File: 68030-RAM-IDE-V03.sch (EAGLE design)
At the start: 73 parts, among them IC1 REG1117, IC10 ICS570B, IC2 74HCT245PW, IC3 74AC16245, IC4 AM29F010S, IC5 74ALVT16543, IC6 74ALVT16543, IC7 XC95288XL-TQ144, IC8 K4S56163, IC9 K4S56163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

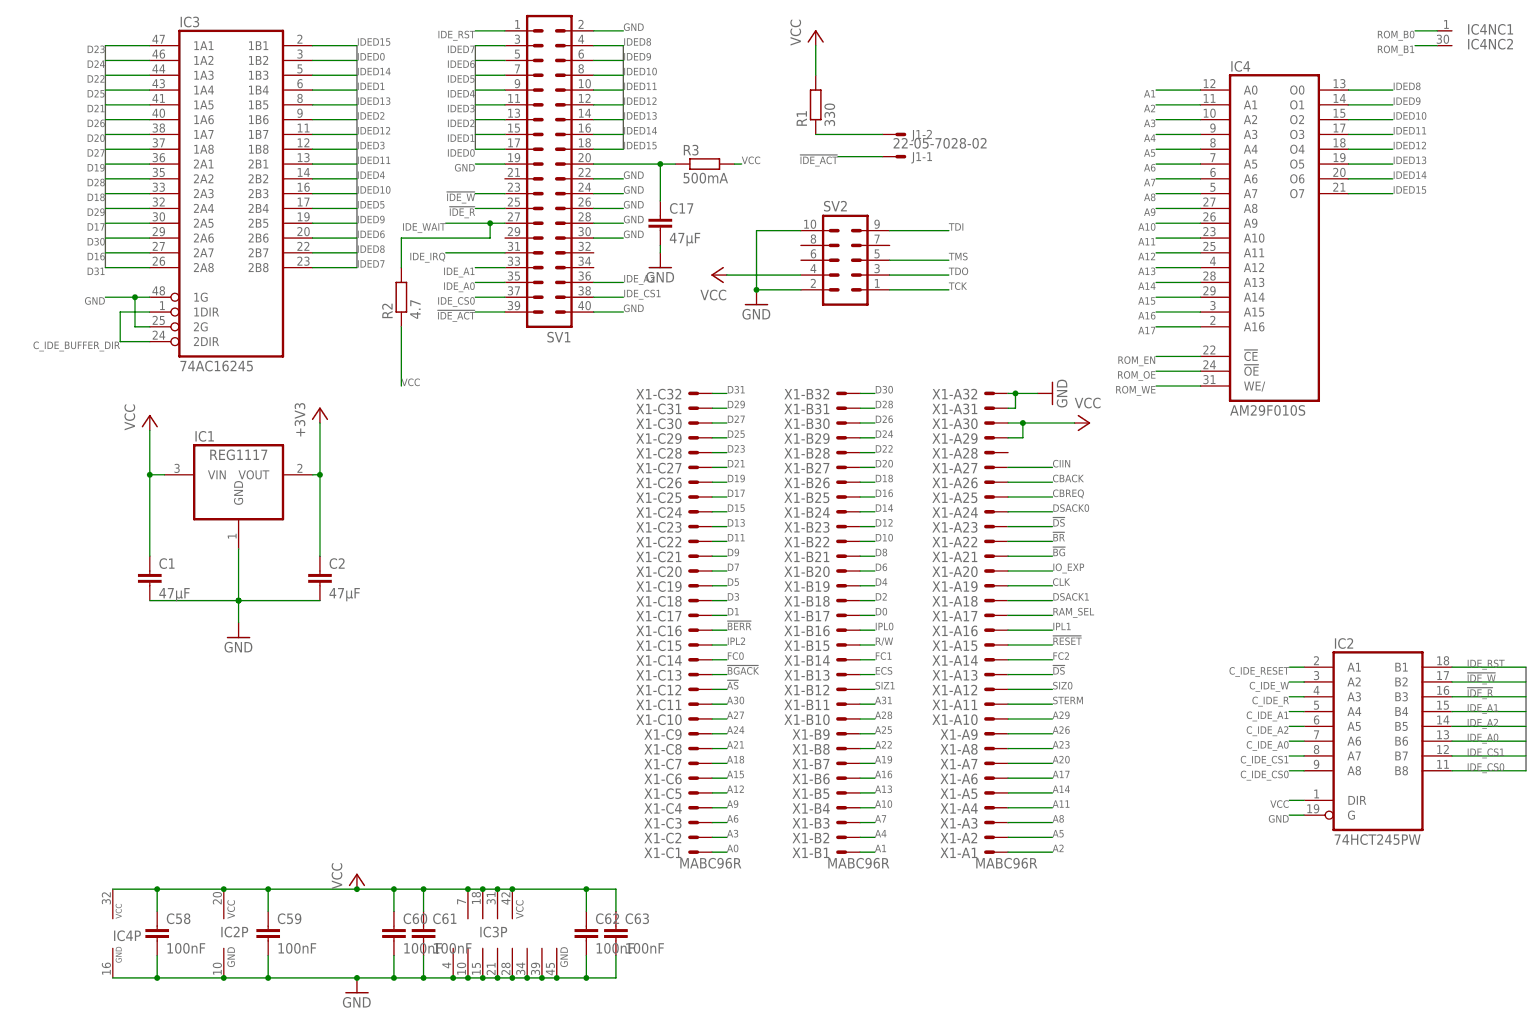
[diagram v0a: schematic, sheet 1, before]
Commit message: Cleaned ARAM/BA signals
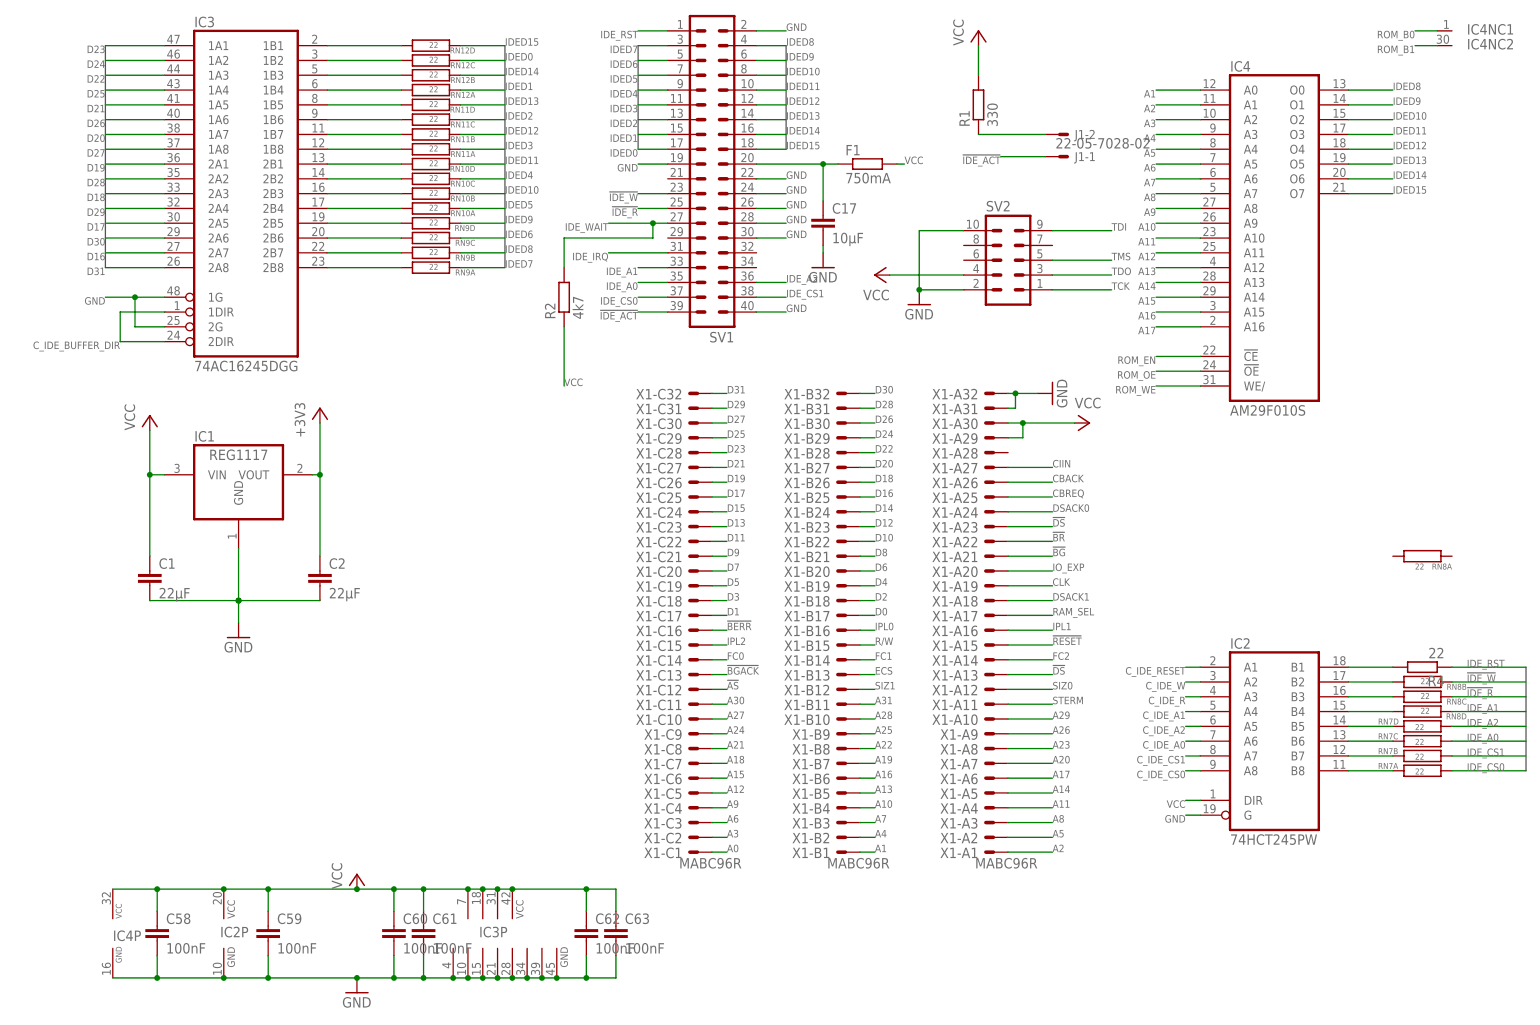
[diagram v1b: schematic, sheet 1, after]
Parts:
- removed R3: 500mA, rcl:R-EU_R2512
- added F1: 750mA, rcl:R-EU_R2512
- added RN1, RN10, RN11, RN12, RN7, RN8, RN9: 22, SMD:R-NETZ@3
- C1, C2: value 47µF -> 22µF; device rcl:C-EUC0805K -> rcl:C-EUC1210K
- C10, C11, C12, C13, C14, C15, C16, C3, C4, C5, C6, C7, C8, C9: device SMD:C-0805-K -> rcl:C-EUC0805K
- C17: value 47µF -> 10µF
- C18, C19, C20, C21, C22, C31, C32, C33, C34, C35, C37, C38, C58, C59, C60, C61, C62, C63: device rcl:C-EUC0603K -> rcl:C-EUC0805K
- C23, C24, C25, C26, C27, C28, C29, C30: value 10nF -> 100nF; device SMD:C-0603-K@3 -> rcl:C-EUC0805K
- C36: value (none) -> 100nF; device rcl:C-EUC0603K -> rcl:C-EUC0805K
- IC3: value 74AC16245 -> 74AC16245DGG; device 74ac-logic:74AC16245 -> 74ac-logic:74AC16245DGG
- IC5, IC6: value 74ALVT16543 -> 74LVTH16543
- R1, R10, R11, R12, R13: device rcl:R-EU_R0603 -> rcl:R-EU_R0805
- R2: value 4.7 -> 4k7; device rcl:R-EU_R0603 -> rcl:R-EU_R0805
- R4: value 33R -> 22; device SMD:R-NETZ@3 -> rcl:R-EU_R0805
- RN2, RN3, RN4, RN5, RN6: value 33R -> 22
- renumbered R5 to RN2, R6 to RN3, R7 to RN4, R8 to RN5, R9 to RN6
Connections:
- new net N$10: IC2A.B4, RN8D.P$1
- new net N$11: IC2A.B1, R4.2
- new net N$12: IC2A.B2, RN8B.P$1
- new net N$13: IC3G$1.1B3, RN12B.P$1
- new net N$14: IC3G$1.1B4, RN12A.P$1
- new net N$15: IC3G$1.1B1, RN12D.P$1
- new net N$16: IC3G$1.1B2, RN12C.P$1
- new net N$17: IC3G$1.1B7, RN11B.P$1
- new net N$18: IC3G$1.1B8, RN11A.P$1
- new net N$19: IC3G$1.1B5, RN11D.P$1
- new net N$2: IC2A.B7, RN7B.P$2
- new net N$20: IC3G$1.1B6, RN11C.P$1
- new net N$21: IC3G$1.2B3, RN10B.P$1
- new net N$22: IC3G$1.2B4, RN10A.P$1
- new net N$23: IC3G$1.2B1, RN10D.P$1
- new net N$24: IC3G$1.2B2, RN10C.P$1
- new net N$27: IC3G$1.2B7, RN9B.P$1
- new net N$28: IC3G$1.2B8, RN9A.P$1
- new net N$29: IC3G$1.2B5, RN9D.P$1
- new net N$3: IC2A.B8, RN7A.P$2
- new net N$30: IC3G$1.2B6, RN9C.P$1
- new net N$6: IC2A.B5, RN7D.P$2
- new net N$7: IC2A.B6, RN7C.P$2
- new net N$9: IC2A.B3, RN8C.P$1
- net !IDE_R: now also RN8C.P$2; no longer IC2A.B3
- net !IDE_W: now also RN8B.P$2; no longer IC2A.B2
- net ARAM_2: now also RN1B.P$1; no longer R4B.P$1
- net ARAM_3: now also RN1D.P$1; no longer R4D.P$1
- net ARAM_4: now also RN1C.P$1; no longer R4C.P$1
- net ARAM_5: now also RN1A.P$1; no longer R4A.P$1
- net C_ARAM_2: now also RN1B.P$2; no longer R4B.P$2
- net C_ARAM_3: now also RN1D.P$2; no longer R4D.P$2
- net C_ARAM_4: now also RN1C.P$2; no longer R4C.P$2
- net C_ARAM_5: now also RN1A.P$2; no longer R4A.P$2
- net IDED0: now also RN12C.P$2; no longer IC3G$1.1B2
- net IDED1: now also RN12A.P$2; no longer IC3G$1.1B4
- net IDED10: now also RN10B.P$2; no longer IC3G$1.2B3
- net IDED11: now also RN10D.P$2; no longer IC3G$1.2B1
- net IDED12: now also RN11B.P$2; no longer IC3G$1.1B7
- net IDED13: now also RN11D.P$2; no longer IC3G$1.1B5
- net IDED14: now also RN12B.P$2; no longer IC3G$1.1B3
- net IDED15: now also RN12D.P$2; no longer IC3G$1.1B1
- net IDED2: now also RN11C.P$2; no longer IC3G$1.1B6
- net IDED3: now also RN11A.P$2; no longer IC3G$1.1B8
- net IDED4: now also RN10C.P$2; no longer IC3G$1.2B2
- net IDED5: now also RN10A.P$2; no longer IC3G$1.2B4
- net IDED6: now also RN9C.P$2; no longer IC3G$1.2B6
- net IDED7: now also RN9A.P$2; no longer IC3G$1.2B8
- net IDED8: now also RN9B.P$2; no longer IC3G$1.2B7
- net IDED9: now also RN9D.P$2; no longer IC3G$1.2B5
- net IDE_A0: now also RN7C.P$1; no longer IC2A.B6
- net IDE_A1: now also RN8D.P$2; no longer IC2A.B4
- net IDE_A2: now also RN7D.P$1; no longer IC2A.B5
- net IDE_CS0: now also RN7A.P$1; no longer IC2A.B8
- net IDE_CS1: now also RN7B.P$1; no longer IC2A.B7
- net IDE_RST: now also R4.1; no longer IC2A.B1
- net IO_EXP: no longer IC7.P$38-FB5MC08/GCK3
- net KEY_PIN_POWER: now also F1.1; no longer R3.1
- net PLL_CLK_FULL: now also IC7.P$38-FB5MC08/GCK3
- net VCC: now also F1.2; no longer R3.2
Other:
- moved on the sheet: C10, C11, C12, C13, C14, C15, C16, C17, C23, C24, C25, C26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

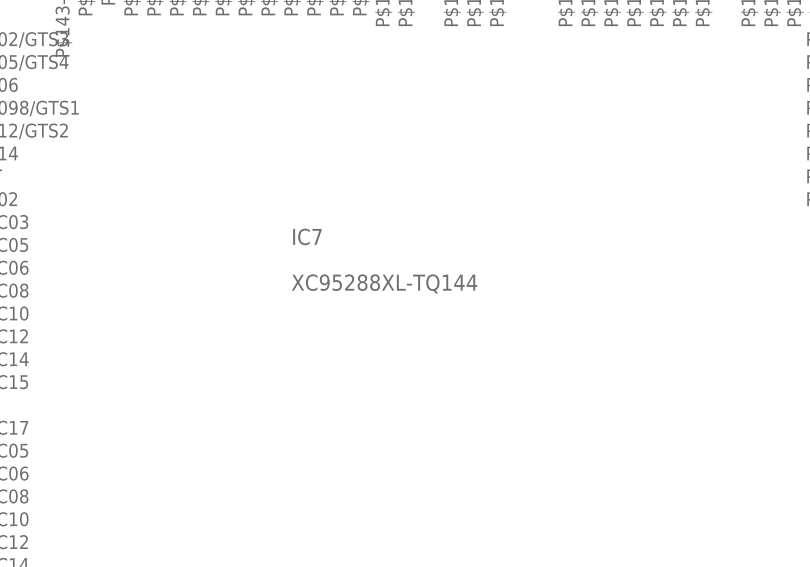
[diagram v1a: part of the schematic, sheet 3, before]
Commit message: Updated the schematics for actual parts
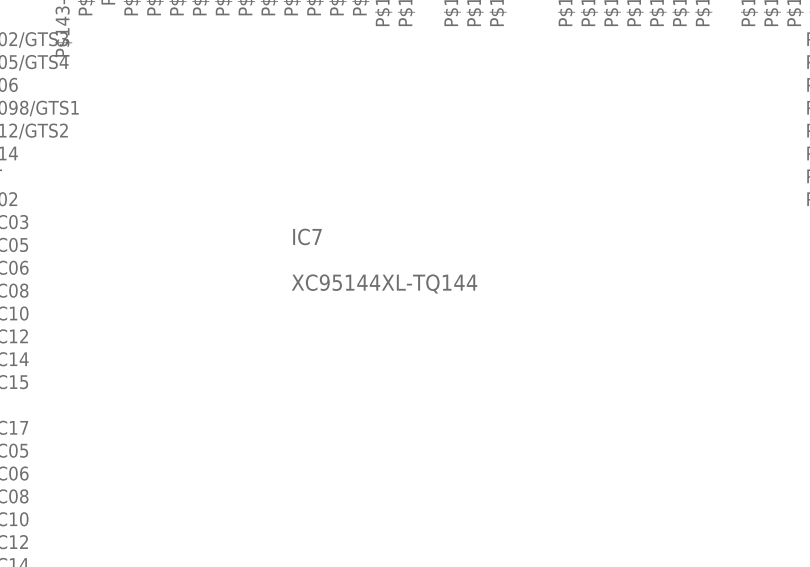
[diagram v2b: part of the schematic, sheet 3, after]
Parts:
- IC7: value XC95288XL-TQ144 -> XC95144XL-TQ144
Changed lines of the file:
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@@
 <part name="GND10" library="SUPPLY1" deviceset="GND" device=""/>
 <part name="IC1" library="burr-brown" deviceset="REG1117" device=""/>
-<part name="IC7" library="xilinx_xc9572xl-tq100" deviceset="XC95288XL-TQ144" device=""/>
+<part name="IC7" library="xilinx_xc9572xl-tq100" deviceset="XC95288XL-TQ144" device="" value="XC95144XL-TQ144"/>
 <part name="C18" library="rcl" deviceset="C-EU" device="C0805K" value="100nF"/>
 <part name="C19" library="rcl" deviceset="C-EU" device="C0805K" value="100nF"/>

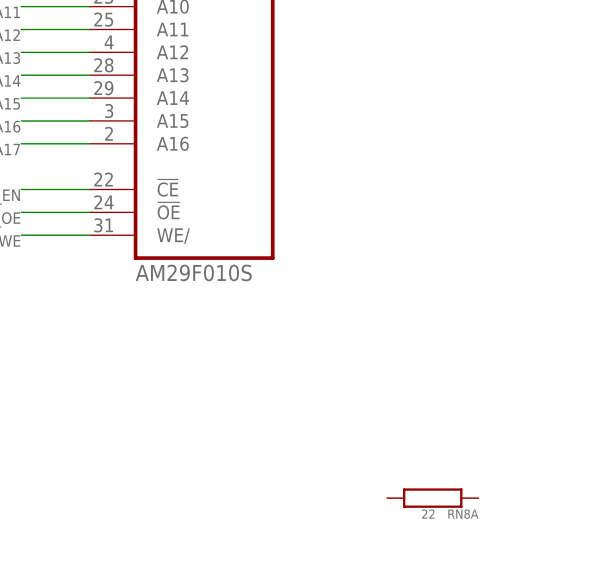
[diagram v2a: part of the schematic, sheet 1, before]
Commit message: Added a JTAG-Pullup
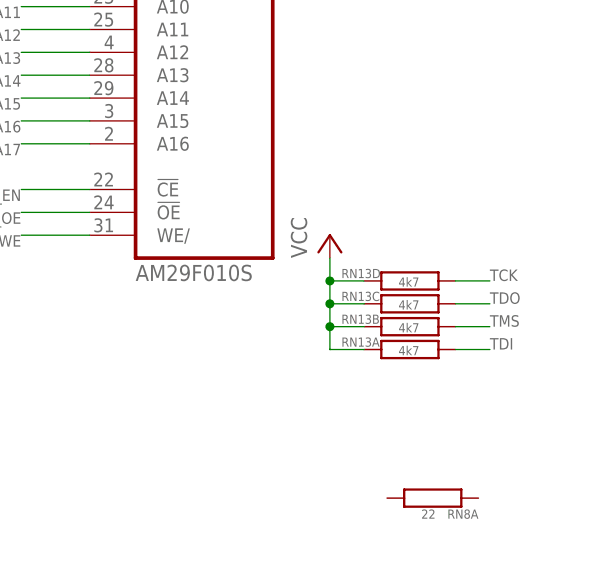
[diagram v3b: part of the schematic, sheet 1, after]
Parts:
- added RN13: 4k7, SMD:R-NETZ@3
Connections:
- net TCK: now also RN13D.P$1
- net TDI: now also RN13A.P$1
- net TDO: now also RN13C.P$1
- net TMS: now also RN13B.P$1
- net VCC: now also RN13A.P$2, RN13B.P$2, RN13C.P$2, RN13D.P$2
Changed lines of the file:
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@@
 <setting verticaltext="up"/>
 </settings>
-<grid distance="0.1" unitdist="inch" unit="inch" style="lines" multiple="1" display="no" altdistance="0.01" altunitdist="inch" altunit="inch"/>
+<grid distance="0.05" unitdist="inch" unit="inch" style="lines" multiple="1" display="no" altdistance="0.01" altunitdist="inch" altunit="inch"/>
 <layers>
 <layer number="1" name="Top" color="4" fill="1" visible="no" active="no"/>
@@
 <part name="RN8" library="SMD" deviceset="R-NETZ@3" device="" value="22"/>
 <part name="R4" library="rcl" deviceset="R-EU_" device="R0805" value="22"/>
+<part name="RN13" library="SMD" deviceset="R-NETZ@3" device="" value="4k7"/>
+<part name="P+7" library="SUPPLY1" deviceset="VCC" device=""/>
 </parts>
 <sheets>
@@
 <instance part="RN8" gate="A" x="236.22" y="81.28" rot="R90"/>
 <instance part="R4" gate="G$1" x="236.22" y="62.23" rot="R180"/>
+<instance part="RN13" gate="B" x="233.68" y="100.33" smashed="yes" rot="R270">
+<attribute name="NAME" x="226.06" y="100.6475" size="1.016" layer="95"/>
+<attribute name="VALUE" x="232.41" y="99.695" size="1.016" layer="96"/>
+</instance>
+<instance part="RN13" gate="A" x="233.68" y="97.79" smashed="yes" rot="R270">
+<attribute name="NAME" x="226.06" y="98.1075" size="1.016" layer="95"/>
+<attribute name="VALUE" x="232.41" y="97.155" size="1.016" layer="96"/>
+</instance>
+<instance part="RN13" gate="D" x="233.68" y="105.41" smashed="yes" rot="R270">
+<attribute name="NAME" x="226.06" y="105.7275" size="1.016" layer="95"/>
+<attribute name="VALUE" x="232.41" y="104.775" size="1.016" layer="96"/>
+</instance>
+<instance part="RN13" gate="C" x="233.68" y="102.87" smashed="yes" rot="R270">
+<attribute name="NAME" x="226.06" y="103.1875" size="1.016" layer="95"/>
+<attribute name="VALUE" x="232.41" y="102.235" size="1.016" layer="96"/>
+</instance>
+<instance part="P+7" gate="VCC" x="224.79" y="110.49"/>
 </instances>
 <busses>
@@
 <junction x="53.34" y="24.13"/>
 </segment>
+<segment>
+<pinref part="RN13" gate="D" pin="P$2"/>
+<wire x1="228.6" y1="105.41" x2="224.79" y2="105.41" width="0.1524" layer="91"/>
+<wire x1="224.79" y1="105.41" x2="224.79" y2="107.95" width="0.1524" layer="91"/>
+<pinref part="RN13" gate="C" pin="P$2"/>
+<wire x1="228.6" y1="102.87" x2="224.79" y2="102.87" width="0.1524" layer="91"/>
+<wire x1="224.79" y1="102.87" x2="224.79" y2="105.41" width="0.1524" layer="91"/>
+<junction x="224.79" y="105.41"/>
+<pinref part="RN13" gate="B" pin="P$2"/>
+<wire x1="228.6" y1="100.33" x2="224.79" y2="100.33" width="0.1524" layer="91"/>
+<wire x1="224.79" y1="100.33" x2="224.79" y2="102.87" width="0.1524" layer="91"/>
+<junction x="224.79" y="102.87"/>
+<pinref part="RN13" gate="A" pin="P$2"/>
+<wire x1="228.6" y1="97.79" x2="224.79" y2="97.79" width="0.1524" layer="91"/>
+<wire x1="224.79" y1="97.79" x2="224.79" y2="100.33" width="0.1524" layer="91"/>
+<junction x="224.79" y="100.33"/>
+<pinref part="P+7" gate="VCC" pin="VCC"/>
+</segment>
 </net>
 <net name="CIIN" class="0">
@@
 <label x="182.88" y="127" size="1.27" layer="95"/>
 </segment>
+<segment>
+<pinref part="RN13" gate="D" pin="P$1"/>
+<wire x1="238.76" y1="105.41" x2="242.57" y2="105.41" width="0.1524" layer="91"/>
+<label x="242.57" y="105.41" size="1.27" layer="95"/>
+</segment>
 </net>
 <net name="TDO" class="0">
@@
 <label x="182.88" y="129.54" size="1.27" layer="95"/>
 </segment>
+<segment>
+<pinref part="RN13" gate="C" pin="P$1"/>
+<wire x1="238.76" y1="102.87" x2="242.57" y2="102.87" width="0.1524" layer="91"/>
+<label x="242.57" y="102.87" size="1.27" layer="95"/>
+</segment>
 </net>
 <net name="TMS" class="0">
@@
 <label x="182.88" y="132.08" size="1.27" layer="95"/>
 </segment>
+<segment>
+<pinref part="RN13" gate="B" pin="P$1"/>
+<wire x1="238.76" y1="100.33" x2="242.57" y2="100.33" width="0.1524" layer="91"/>
+<label x="242.57" y="100.33" size="1.27" layer="95"/>
+</segment>
 </net>
 <net name="TDI" class="0">
@@
 <label x="182.88" y="137.16" size="1.27" layer="95"/>
 </segment>
-</net>
+<segment>
+<pinref part="RN13" gate="A" pin="P$1"/>
+<wire x1="238.76" y1="97.79" x2="242.57" y2="97.79" width="0.1524" layer="91"/>
+<label x="242.57" y="97.79" size="1.27" layer="95"/>
+</segment>
+</net>
